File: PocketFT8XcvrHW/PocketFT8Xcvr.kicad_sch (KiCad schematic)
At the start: 54 parts, among them IC1 SI5351C-B-GM1, J1 HX8357D SPI, J2 22-23-2021, J3 GPS, J5 HX8357D 8-BIT, Q1 2N3904, Q2 2N3906, Q3 2N7000, Q4 2N7000, U1 MCP3422A1T-E/SN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

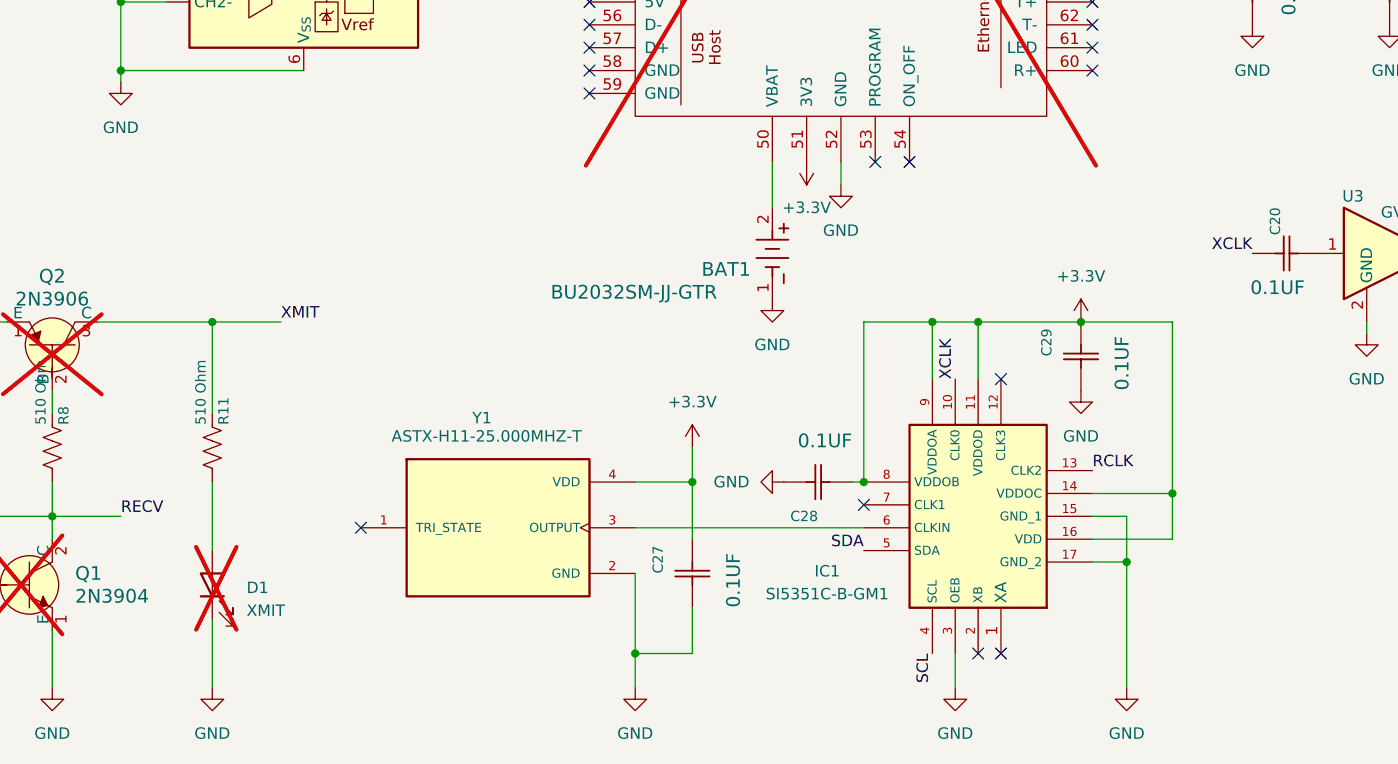
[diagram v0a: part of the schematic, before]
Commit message: Housecleaning after abandoning the QFN16 SI5351 package
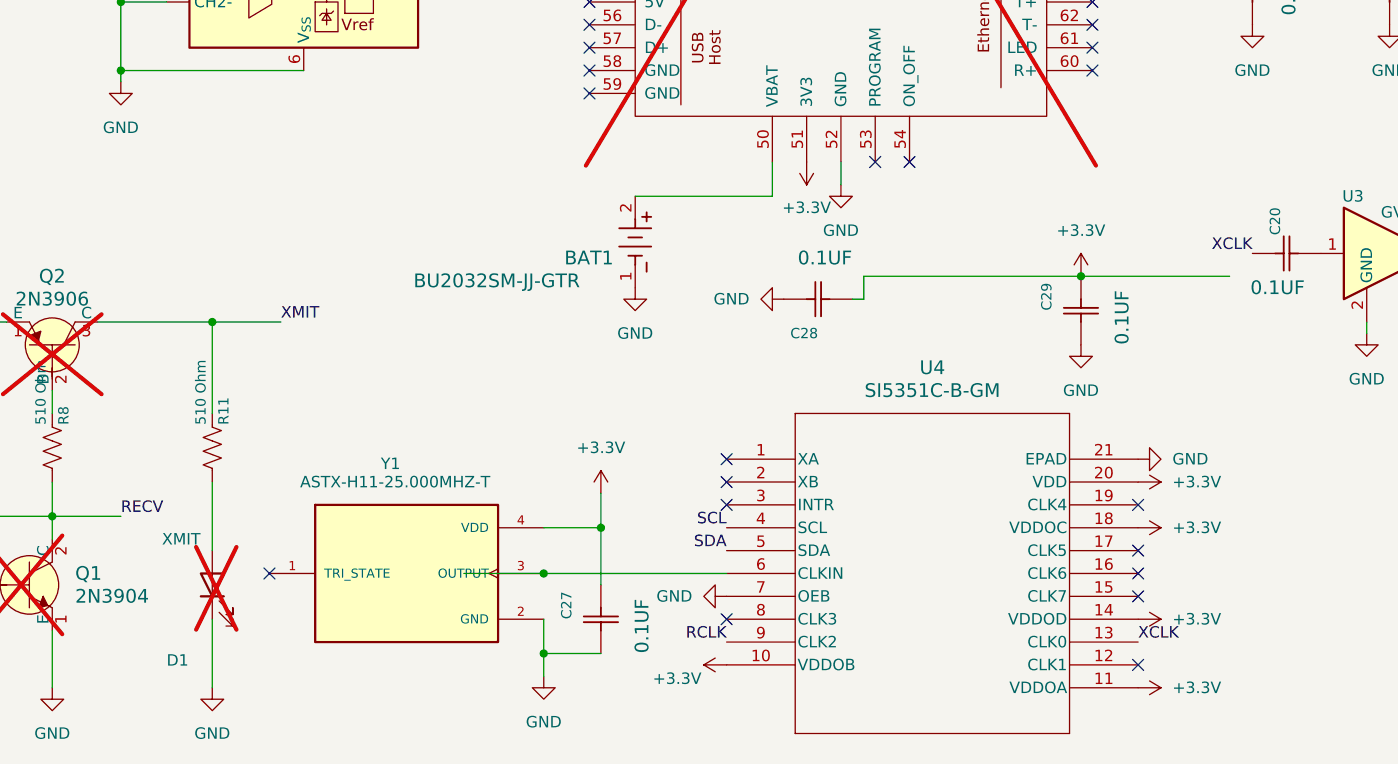
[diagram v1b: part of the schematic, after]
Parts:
- removed IC1: SI5351C-B-GM1, SI5351C-B-GM1:QFN50P300X300X90-17N-D, symbol SI5351C-B-GM1:SI5351C-B-GM1
- added U4: SI5351C-B-GM, QFN20_4X4_SKY, symbol 2024-08-12_00-43-20:SI5351C-B-GM
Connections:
- net +3.3V: now also U4.10 (VDDOB), U4.11 (VDDOA), U4.14 (VDDOD), U4.18 (VDDOC), U4.20 (VDD)
- net GND: now also U4.21 (EPAD), U4.7 (OEB)
- net RCLK: now also U4.9 (CLK2)
- net SCL: now also U4.4 (SCL)
- net SDA: now also U4.5 (SDA)
- net XCLK: now also U4.13 (CLK0)
- net at Y1.3 (OUTPUT): now also U4.6 (CLKIN)
- no-connect marks 78 -> 83
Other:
- moved on the sheet: BAT1, C27, C28, C29, Y1

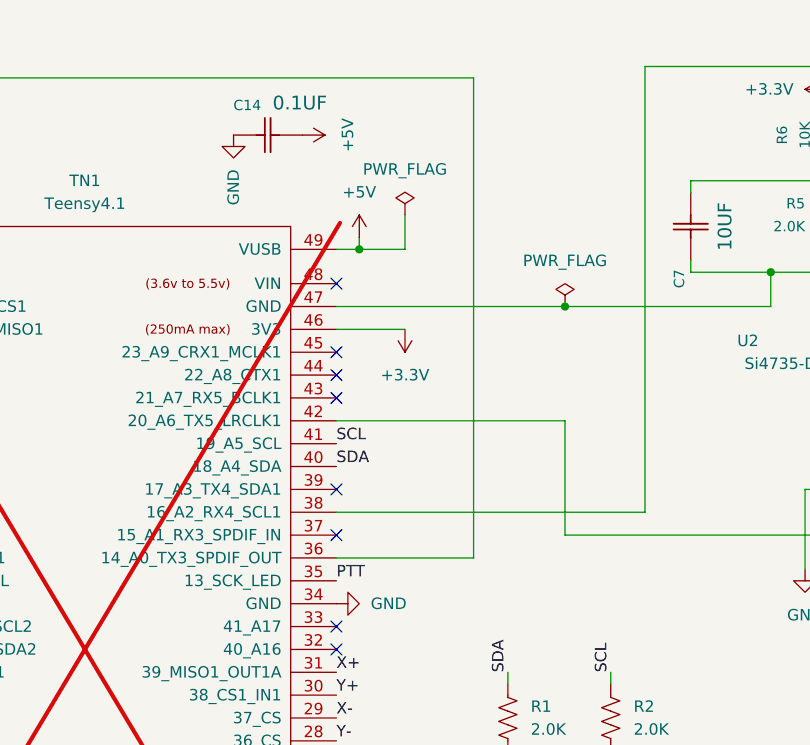
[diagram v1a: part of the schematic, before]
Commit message: PCB Patch, test and FW changes to repair 1-v101-sck-and-ptt-reversed
SCK signal moved from digital pin 14 in Teensy 3.6 to pin 13 in Teensy 4.1.  Workaround PCB patch swaps pins 13 and 14.  Schematic, board layout, tests and FW updated for revised pin assignments.  Test03-Display now passes.
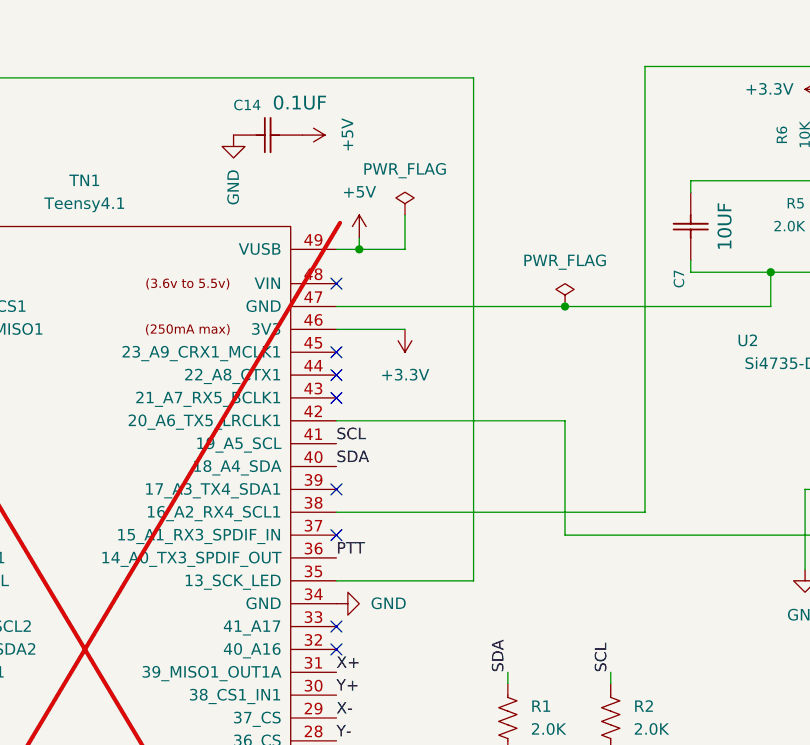
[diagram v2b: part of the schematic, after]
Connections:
- net DCLK: now also TN1.35 (13_SCK_LED); no longer TN1.36 (14_A0_TX3_SPDIF_OUT)
- net PTT: now also TN1.36 (14_A0_TX3_SPDIF_OUT); no longer TN1.35 (13_SCK_LED)
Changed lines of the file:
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@@
-	(wire
-		(pts
-			(xy 175.26 74.93) (xy 175.26 21.59)
-		)
-		(stroke
-			(width 0)
-			(type default)
-		)
-	)
 	(wire
 		(pts
@@
 	(wire
 		(pts
-			(xy 160.02 74.93) (xy 175.26 74.93)
-		)
-		(stroke
-			(width 0)
-			(type default)
-		)
-	)
-	(wire
-		(pts
 			(xy 62.23 167.64) (xy 62.23 175.26)
 		)
@@
 	(wire
 		(pts
+			(xy 160.02 77.47) (xy 175.26 77.47)
+		)
+		(stroke
+			(width 0)
+			(type default)
+		)
+	)
+	(wire
+		(pts
 			(xy 199.39 33.02) (xy 199.39 34.29)
 		)
@@
 		(pts
 			(xy 38.1 85.09) (xy 38.1 87.63)
+		)
+		(stroke
+			(width 0)
+			(type default)
+		)
+	)
+	(wire
+		(pts
+			(xy 175.26 21.59) (xy 175.26 77.47)
 		)
 		(stroke
@@
 		)
 	)
+	(label "PTT"
+		(at 160.02 74.93 0)
+		(fields_autoplaced yes)
+		(effects
+			(font
+				(size 1.27 1.27)
+			)
+			(justify left bottom)
+		)
+	)
 	(label "SDA"
 		(at 160.02 64.77 0)
@@
 		(fields_autoplaced yes)
 		(effects
-			(font
-				(size 1.27 1.27)
-			)
-			(justify left bottom)
-		)
-	)
-	(label "PTT"
-		(at 160.02 77.47 0)
-		(fields_autoplaced yes)
-		(effects

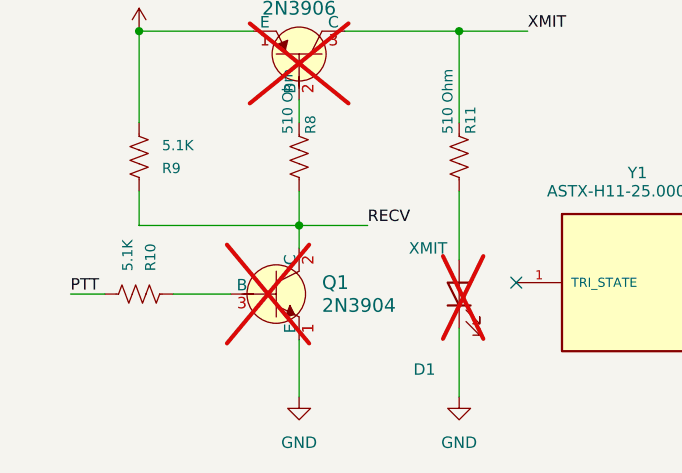
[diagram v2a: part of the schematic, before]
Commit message: Fixed XMIT LED is always "on" and cannot be turned-off
The digikey 2N3904 symbol reversed the pin numbers for B and C.  This commit includes the schematic with the corrected symbol.
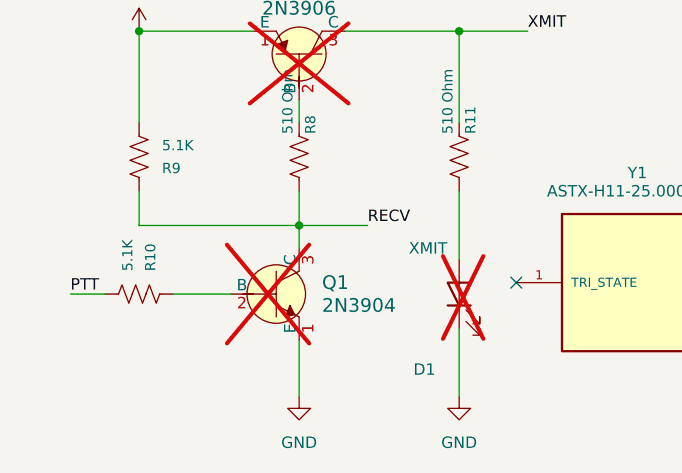
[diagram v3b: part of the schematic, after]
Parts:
- Q1: MPN (none) -> 2N3904
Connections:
- net RECV: now also Q1.3 (C); no longer Q1.2 (C)
- net at R10.1: now also Q1.2 (B); no longer Q1.3 (B)
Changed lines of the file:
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@@
+			)
+		)
+		(property "MPN" "2N3904"
+			(at 46.99 166.37 0)
+			(effects
+				(font
+					(size 1.524 1.524)
+				)
+				(justify left)
+				(hide yes)
 			)
 		)

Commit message: Resolved:  Touchpad needs coordination over full screen #8
Added R12 and R13 to lower the driven voltage to the touchpad so that it lies below the MCP3422's 2.048 Volt reference.
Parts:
- added R12, R13: 510, Resistor_SMD:R_0603_1608Metric, symbol SparkFun-Resistor:2.0k_0603
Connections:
- net X-: now also R12.2; no longer J1.7 (X-)
- net Y+: now also R13.2; no longer J1.10 (Y+)
- new net: J1.7 (X-), R12.1
- new net: J1.10 (Y+), R13.1
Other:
- moved on the sheet: R1, R2

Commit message: Resolve V1.01 PCB is using the Teensy 3.X rather than 4.X audio input network on pin A2 #15
Resolution modifies V1.01 schematic to replace 10K R6 with 2.2K Ohms per Teensy Audio System Design Tool documentation for ADC input on Teensy 4.1.
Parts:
- R6: value 10K -> 2.2K; Mfg Part # RC0603JR-0710KL -> (none); PROD_ID RES-00824 -> (none)
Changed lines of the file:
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@@
 			)
 		)
-		(property "Value" "10K"
+		(property "Value" "2.2K"
 			(at 212.09 27.94 0)
 			(effects
@@
 			)
 		)
-		(property "Datasheet" "https://www.vishay.com/docs/20035/dcrcwe3.pdf"
+		(property "Datasheet" ""
 			(at 223.52 27.94 0)
 			(effects
@@
 			)
 		)
-		(property "Description" "RES 47.0K OHM 1/8W 0805 SMD"
+		(property "Description" ""
 			(at 226.06 27.94 0)
 			(effects
@@
 			)
 		)
-		(property "PROD_ID" "RES-00824"
+		(property "PROD_ID" ""
 			(at 220.98 27.94 0)
 			(effects
@@
 			)
 		)
-		(property "Mfg Part #" "RC0603JR-0710KL"
+		(property "Mfg Part #" ""
 			(at 214.63 27.94 0)
 			(effects

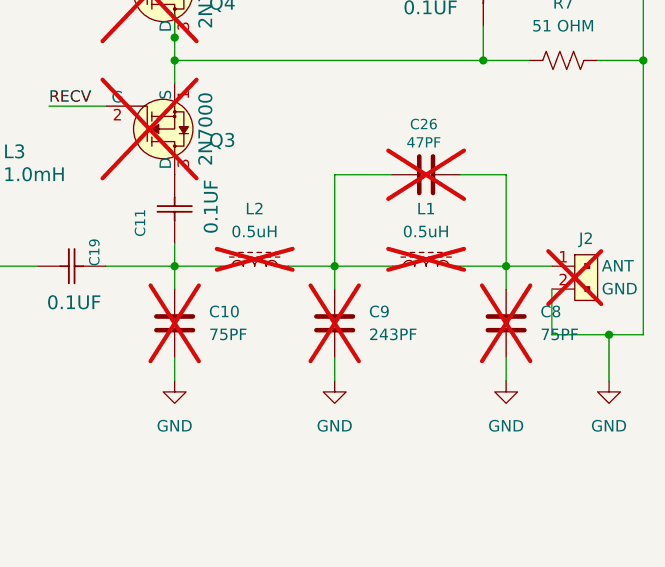
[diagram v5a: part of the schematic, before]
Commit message: Reactive components adjusted for 40M operation
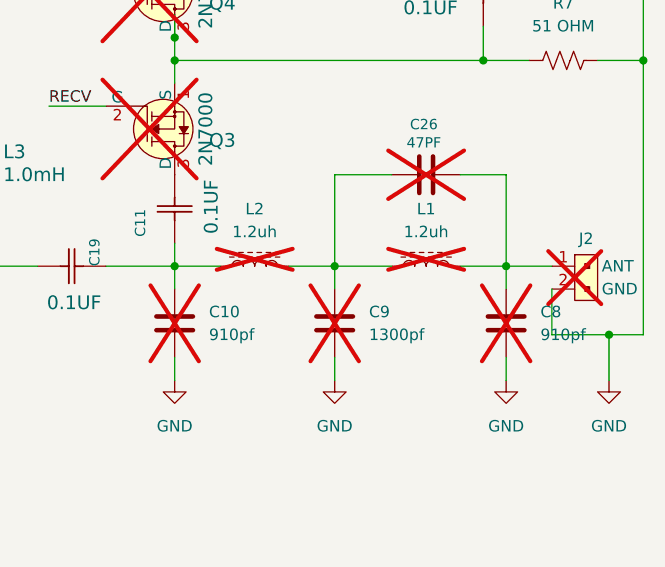
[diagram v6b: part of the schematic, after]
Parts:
- C10, C8: value 75PF -> 910pf
- C9: value 243PF -> 1300pf
- L1, L2: value 0.5uH -> 1.2uh
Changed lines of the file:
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@@
 	(title_block
 		(title "Pocket FT8 Transceiver")
-		(date "2024-07-31")
+		(date "2024-09-30")
 		(rev "1.10")
 		(company "KQ7B")
@@
 			)
 		)
-		(property "Value" "75PF"
+		(property "Value" "910pf"
 			(at 267.97 149.86 0)
 			(effects
@@
 		(exclude_from_sim no)
 		(in_bom no)
-		(on_board yes)
+		(on_board no)
 		(dnp yes)
 		(property "Reference" "C26"
@@
 			)
 		)
-		(property "Value" "0.5uH"
+		(property "Value" "1.2uh"
 			(at 255.27 138.43 90)
 			(effects
@@
 			)
 		)
-		(property "Value" "0.5uH"
+		(property "Value" "1.2uh"
 			(at 236.22 138.43 90)
 			(effects
@@
 		(fields_autoplaced yes)
 		(property "Reference" "C9"
-			(at 248.92 147.32 0)
+			(at 248.92 147.3199 0)
 			(effects
 				(font
@@
 			)
 		)
-		(property "Value" "243PF"
-			(at 248.92 149.86 0)
+		(property "Value" "1300pf"
+			(at 248.92 149.8599 0)
 			(effects
 				(font
@@
 		(fields_autoplaced yes)
 		(property "Reference" "C10"
-			(at 231.14 147.32 0)
+			(at 231.14 147.3199 0)
 			(effects
 				(font
@@
 			)
 		)
-		(property "Value" "75PF"
-			(at 231.14 149.86 0)
+		(property "Value" "910pf"
+			(at 231.14 149.8599 0)
 			(effects
 				(font

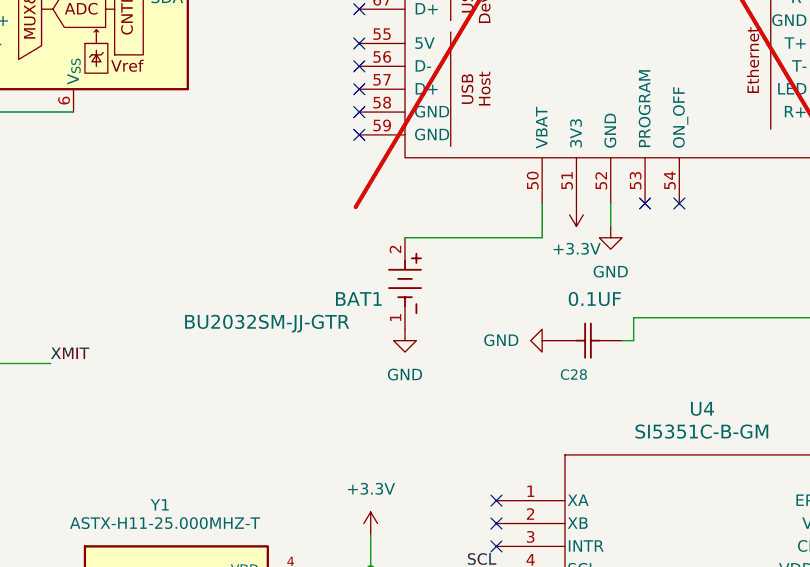
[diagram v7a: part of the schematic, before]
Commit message: Moved battery to back (solder) side of board
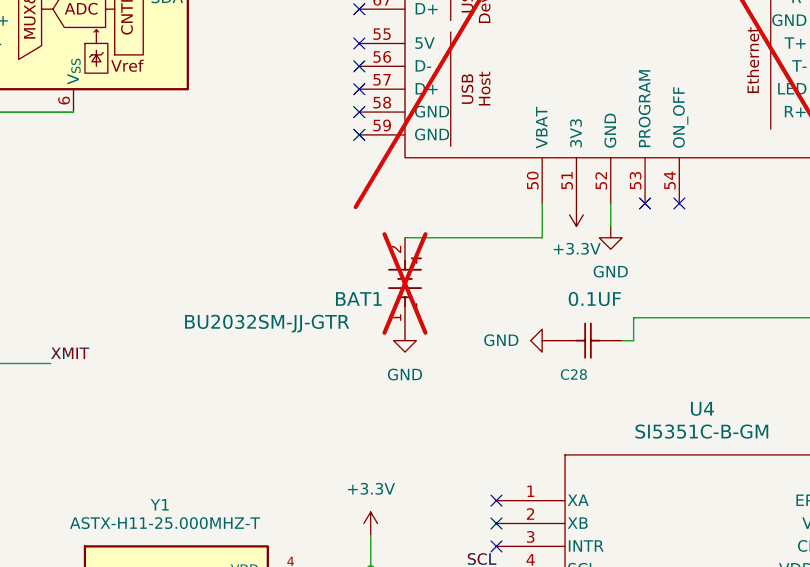
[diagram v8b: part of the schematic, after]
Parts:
- BAT1: now not fitted; now left out of the parts list
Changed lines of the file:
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@@
 		(unit 1)
 		(exclude_from_sim no)
-		(in_bom yes)
+		(in_bom no)
 		(on_board yes)
-		(dnp no)
+		(dnp yes)
 		(property "Reference" "BAT1"
 			(at 101.346 142.748 90)
